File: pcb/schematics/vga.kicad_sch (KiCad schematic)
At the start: 1 part

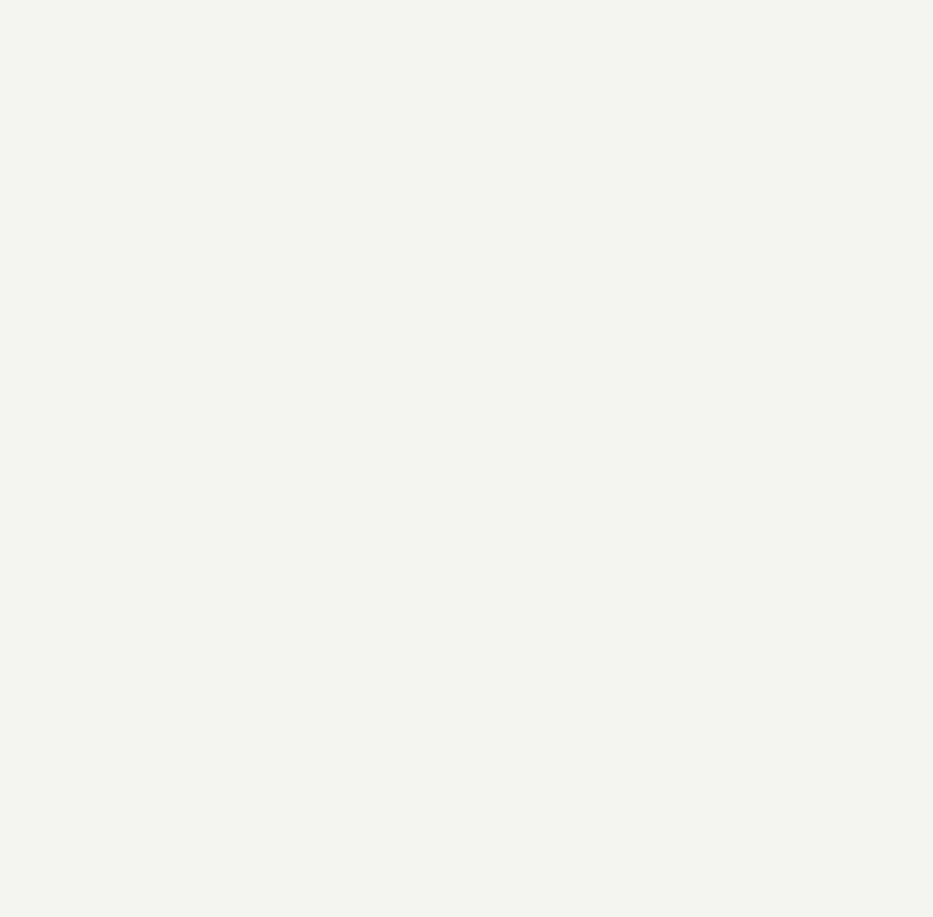
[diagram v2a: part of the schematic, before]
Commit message: add ths8136 symbol
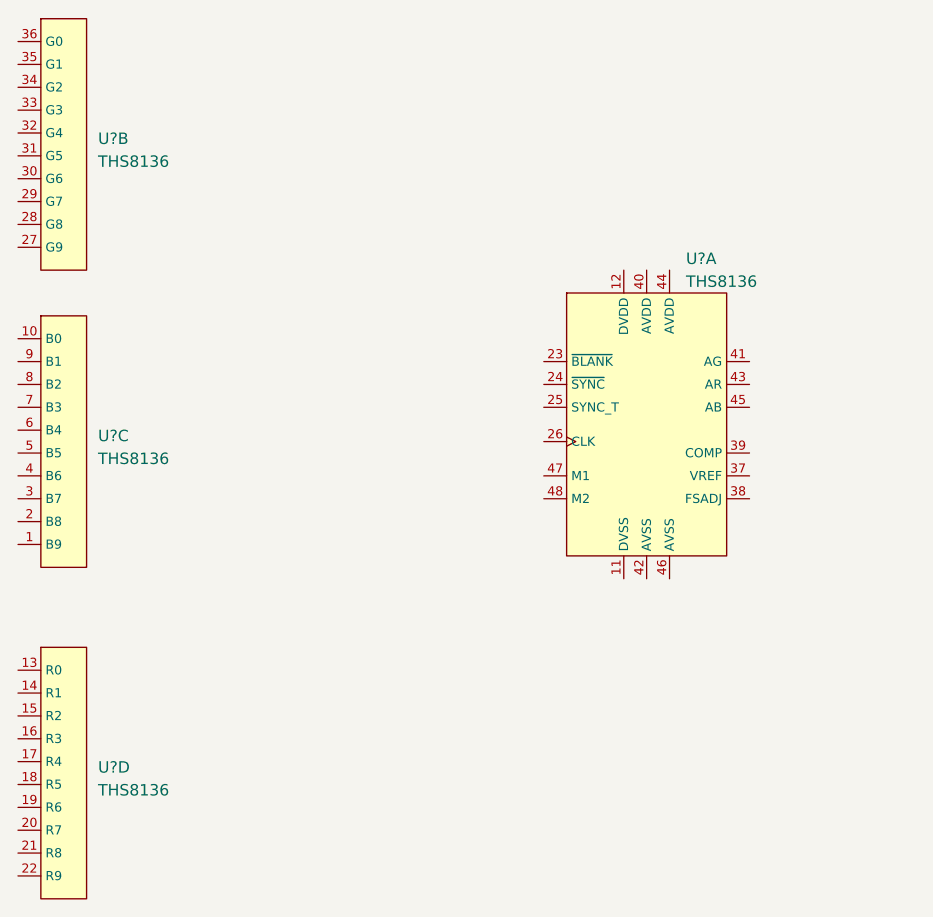
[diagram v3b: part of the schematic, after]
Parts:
- added U? (x4): THS8136, symbol THS8136:THS8136
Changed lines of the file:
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@@
 (kicad_sch (version 20220126) (generator eeschema)
   (paper "A4")
+  (symbol (lib_id "THS8136:THS8136") (at 101.6 138.43 0) (unit 4)
+    (in_bom yes) (on_board yes) (fields_autoplaced)
+    (property "Reference" "U?" (id 0) (at 102.87 127.635 0)
+      (effects (font (size 1.27 1.27)) (justify left))
+    )
+    (property "Value" "THS8136" (id 1) (at 102.87 130.175 0)
+      (effects (font (size 1.27 1.27)) (justify left))
+    )
+    (property "Footprint" "" (id 2) (at 100.33 111.76 0)
+      (effects (font (size 1.27 1.27)) hide)
+    )
+    (property "Datasheet" "" (id 3) (at 100.33 111.76 0)
+      (effects (font (size 1.27 1.27)) hide)
+    )
+    (pin "13")
+    (pin "14")
+    (pin "15")
+    (pin "16")
+    (pin "17")
+    (pin "18")
+    (pin "19")
+    (pin "20")
+    (pin "21")
+    (pin "22")
+  )
+  (symbol (lib_id "THS8136:THS8136") (at 163.83 88.9 0) (unit 1)
+    (in_bom yes) (on_board yes) (fields_autoplaced)
+    (property "Reference" "U?" (id 0) (at 168.1989 71.12 0)
+      (effects (font (size 1.27 1.27)) (justify left))
+    )
+    (property "Value" "THS8136" (id 1) (at 168.1989 73.66 0)
+      (effects (font (size 1.27 1.27)) (justify left))
+    )
+    (property "Footprint" "" (id 2) (at 162.56 62.23 0)
+      (effects (font (size 1.27 1.27)) hide)
+    )
+    (property "Datasheet" "" (id 3) (at 162.56 62.23 0)
+      (effects (font (size 1.27 1.27)) hide)
+    )
+    (pin "11")
+    (pin "12")
+    (pin "23")
+    (pin "24")
+    (pin "25")
+    (pin "26")
+    (pin "37")
+    (pin "38")
+    (pin "39")
+    (pin "40")
+    (pin "41")
+    (pin "42")
+    (pin "43")
+    (pin "44")
+    (pin "45")
+    (pin "46")
+    (pin "47")
+    (pin "48")
+  )
+  (symbol (lib_id "THS8136:THS8136") (at 101.6 68.58 0) (unit 2)
+    (in_bom yes) (on_board yes) (fields_autoplaced)
+    (property "Reference" "U?" (id 0) (at 102.87 57.785 0)
+      (effects (font (size 1.27 1.27)) (justify left))
+    )
+    (property "Value" "THS8136" (id 1) (at 102.87 60.325 0)
+      (effects (font (size 1.27 1.27)) (justify left))
+    )
+    (property "Footprint" "" (id 2) (at 100.33 41.91 0)
+      (effects (font (size 1.27 1.27)) hide)
+    )
+    (property "Datasheet" "" (id 3) (at 100.33 41.91 0)
+      (effects (font (size 1.27 1.27)) hide)
+    )
+    (pin "27")
+    (pin "28")
+    (pin "29")
+    (pin "30")
+    (pin "31")
+    (pin "32")
+    (pin "33")
+    (pin "34")
+    (pin "35")
+    (pin "36")
+  )
+  (symbol (lib_id "THS8136:THS8136") (at 101.6 101.6 0) (unit 3)
+    (in_bom yes) (on_board yes) (fields_autoplaced)
+    (property "Reference" "U?" (id 0) (at 102.87 90.805 0)
+      (effects (font (size 1.27 1.27)) (justify left))
+    )
+    (property "Value" "THS8136" (id 1) (at 102.87 93.345 0)
+      (effects (font (size 1.27 1.27)) (justify left))
+    )
+    (property "Footprint" "" (id 2) (at 100.33 74.93 0)
+      (effects (font (size 1.27 1.27)) hide)
+    )
+    (property "Datasheet" "" (id 3) (at 100.33 74.93 0)
+      (effects (font (size 1.27 1.27)) hide)
+    )
+    (pin "1")
+    (pin "10")
+    (pin "2")
+    (pin "3")
+    (pin "4")
+    (pin "5")
+    (pin "6")
+    (pin "7")
+    (pin "8")
+    (pin "9")
+  )
   (symbol (lib_id "Connector:DB15_Female_HighDensity") (at 226.06 91.44 0) (unit 1)
     (in_bom yes) (on_board yes) (fields_autoplaced)

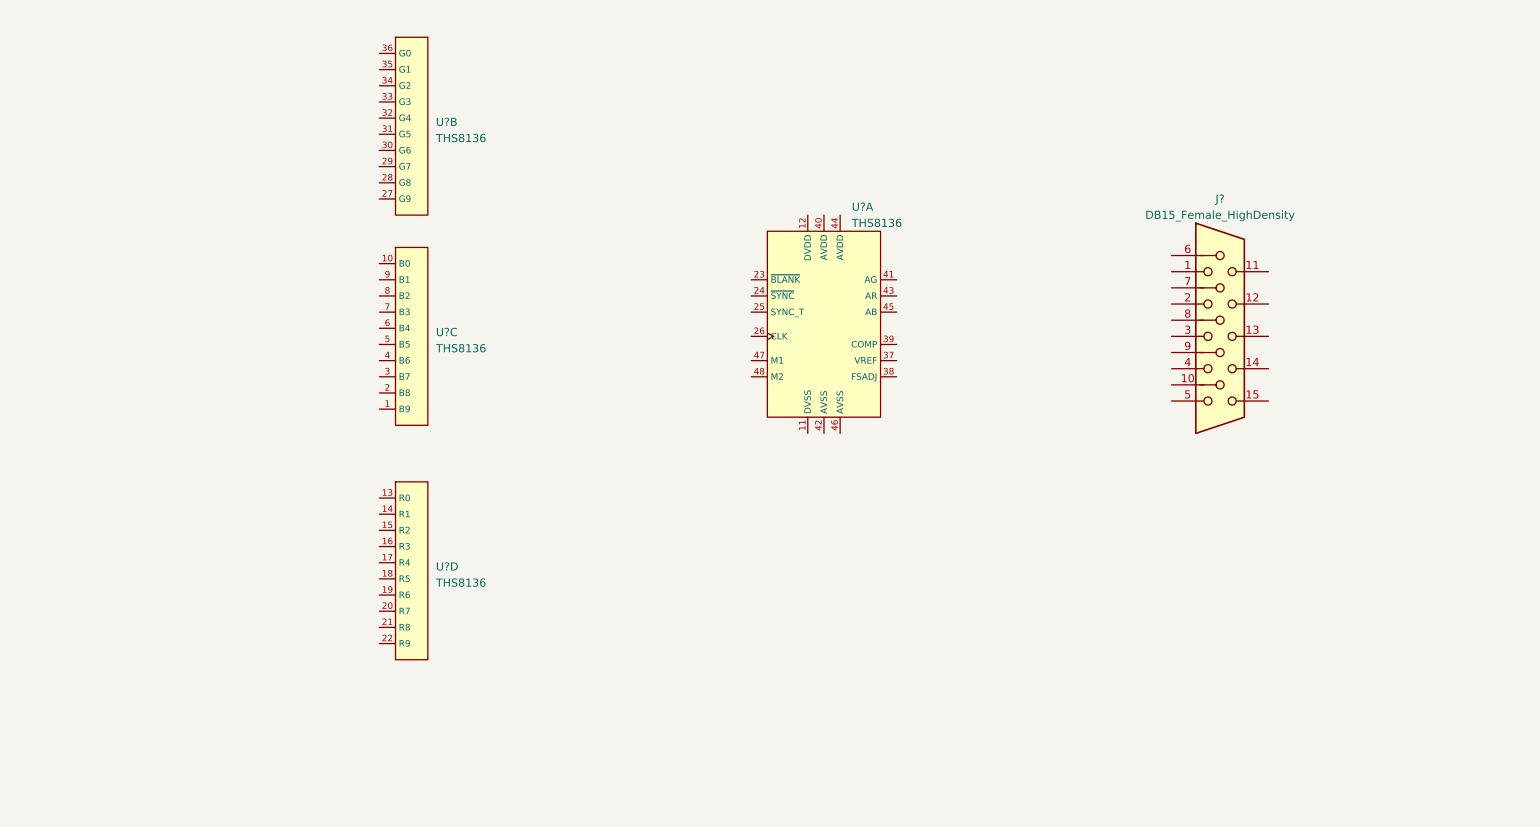
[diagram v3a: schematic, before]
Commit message: add vga frontend
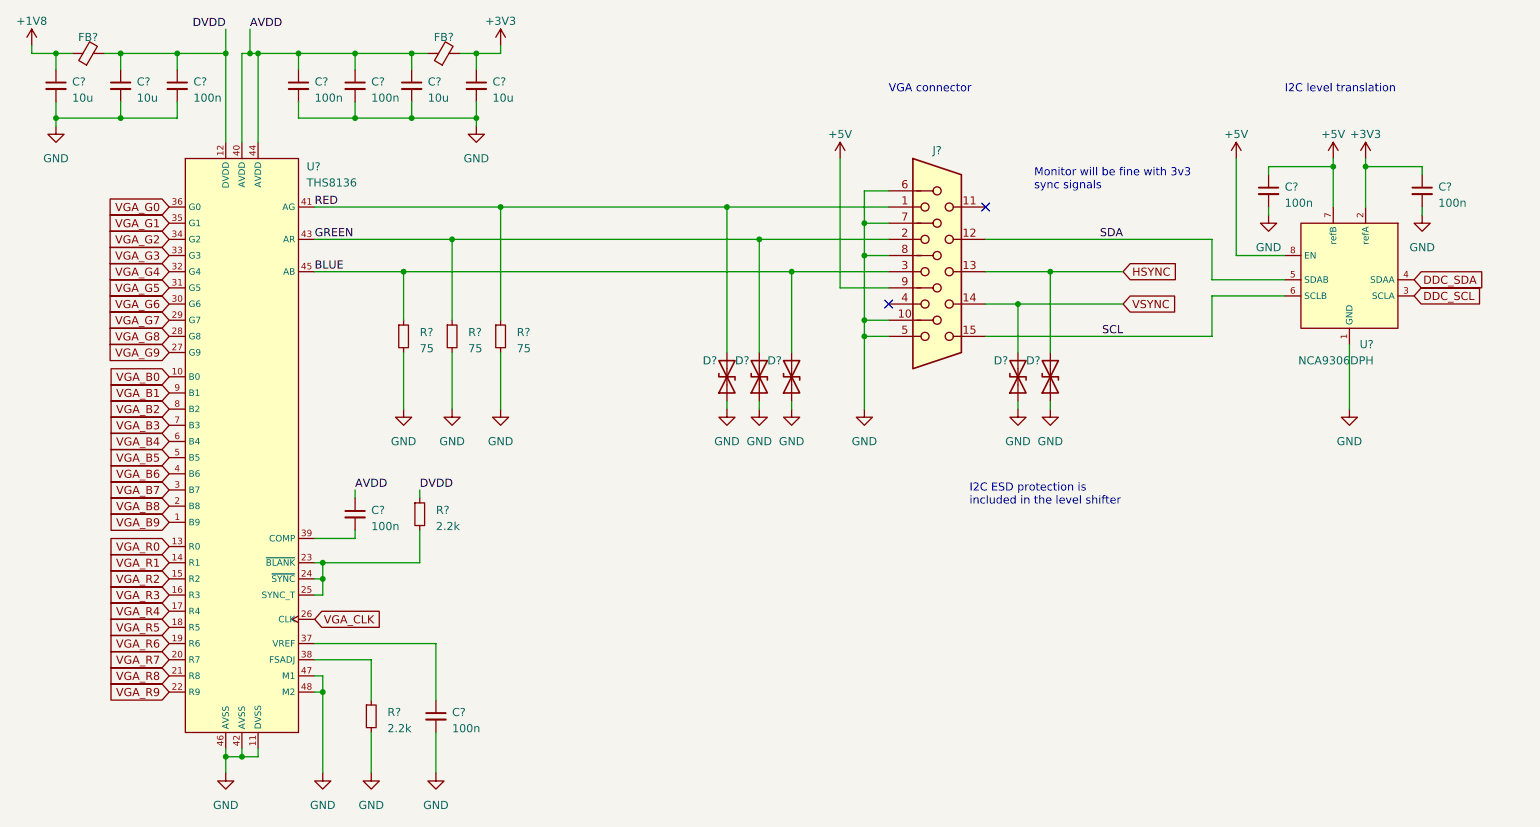
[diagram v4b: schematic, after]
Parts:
- removed U? (x4): THS8136, symbol THS8136:THS8136
- added C? (x4): 10u, symbol Device:C_Small
- added C? (x7): 100n, symbol Device:C_Small
- added D? (x5): D_TVS, symbol Device:D_TVS
- added FB? (x2): FerriteBead_Small, symbol Device:FerriteBead_Small
- added R? (x3): 75, symbol Device:R_Small
- added R? (x2): 2.2k, symbol Device:R_Small
- added U?: NCA9306DPH, symbol NCA9306:NCA9306DPH
- added U?: THS8136, symbol THS8136:THS8136
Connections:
- net RED: now reaches J?.1
- net RED: now also D?.2 (A2), R?.1, U?.41 (AG)
- net GND: now reaches J?.10
- net GND: now also J?.5, J?.6, J?.7, J?.8, C?.2, C?.2, C?.2, C?.2, C?.2, C?.2, C?.2, C?.2, C?.2, C?.2, D?.1 (A1), D?.1 (A1), D?.1 (A1), D?.1 (A1), D?.1 (A1), R?.2, R?.2, R?.2, R?.2, U?.1 (GND), U?.11 (DVSS), U?.42 (AVSS), U?.46 (AVSS), U?.47 (M1), U?.48 (M2)
- net SDA: now reaches J?.12
- net SDA: now also U?.5 (SDAB)
- net HSYNC: now reaches J?.13
- net HSYNC: now also D?.2 (A2)
- net VSYNC: now reaches J?.14
- net VSYNC: now also D?.2 (A2)
- net SCL: now reaches J?.15
- net SCL: now also U?.6 (SCLB)
- net GREEN: now reaches J?.2
- net GREEN: now also D?.2 (A2), R?.1, U?.43 (AR)
- net BLUE: now reaches J?.3
- net BLUE: now also D?.2 (A2), R?.1, U?.45 (AB)
- net +5V: now reaches J?.9
- net +5V: now also C?.1, U?.7 (refB), U?.8 (EN)
- new net: R?.2, U?.23 (~{BLANK}), U?.24 (~{SYNC}), U?.25 (SYNC_T)
- new net: C?.1, U?.37 (VREF)
- new net: R?.1, U?.38 (FSADJ)
- new net: C?.2, U?.39 (COMP)
- new net +1V8: C?.1, FB?.1
- new net +3V3: C?.1, C?.1, FB?.2, U?.2 (refA)
- new net AVDD: C?.1, C?.1, C?.1, C?.1, FB?.1, U?.40 (AVDD), U?.44 (AVDD)
- new net DDC_SCL: U?.3 (SCLA)
- new net DDC_SDA: U?.4 (SDAA)
- new net DVDD: C?.1, C?.1, FB?.2, R?.1, U?.12 (DVDD)
- new net VGA_B0: U?.10 (B0)
- new net VGA_B1: U?.9 (B1)
- new net VGA_B2: U?.8 (B2)
- new net VGA_B3: U?.7 (B3)
- new net VGA_B4: U?.6 (B4)
- new net VGA_B5: U?.5 (B5)
- new net VGA_B6: U?.4 (B6)
- new net VGA_B7: U?.3 (B7)
- new net VGA_B8: U?.2 (B8)
- new net VGA_B9: U?.1 (B9)
- new net VGA_CLK: U?.26 (CLK)
- new net VGA_G0: U?.36 (G0)
- new net VGA_G1: U?.35 (G1)
- new net VGA_G2: U?.34 (G2)
- new net VGA_G3: U?.33 (G3)
- new net VGA_G4: U?.32 (G4)
- new net VGA_G5: U?.31 (G5)
- new net VGA_G6: U?.30 (G6)
- new net VGA_G7: U?.29 (G7)
- new net VGA_G8: U?.28 (G8)
- new net VGA_G9: U?.27 (G9)
- new net VGA_R0: U?.13 (R0)
- new net VGA_R1: U?.14 (R1)
- new net VGA_R2: U?.15 (R2)
- new net VGA_R3: U?.16 (R3)
- new net VGA_R4: U?.17 (R4)
- new net VGA_R5: U?.18 (R5)
- new net VGA_R6: U?.19 (R6)
- new net VGA_R7: U?.20 (R7)
- new net VGA_R8: U?.21 (R8)
- new net VGA_R9: U?.22 (R9)
- no-connect marks 0 -> 2
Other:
- note added: "I2C ESD protection is included in the level shifter"
- note added: "I2C level translation"
- note added: "Monitor will be fine with 3v3 sync signals"
- note added: "VGA connector"
- moved on the sheet: J?

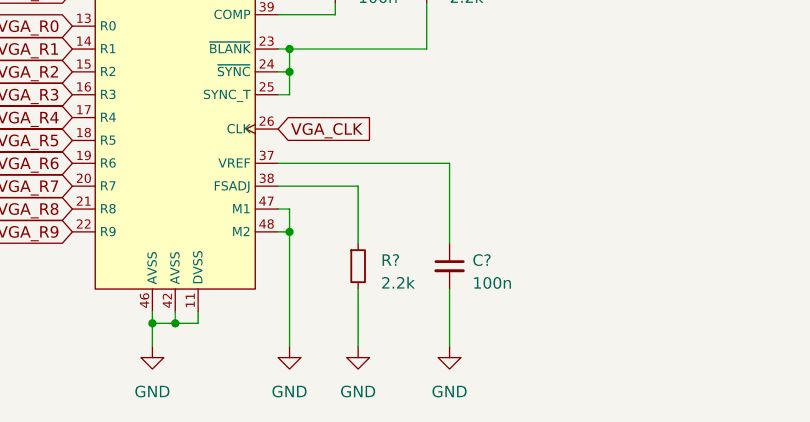
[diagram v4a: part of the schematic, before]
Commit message: fix wrong fasdj resistor on vga frontend
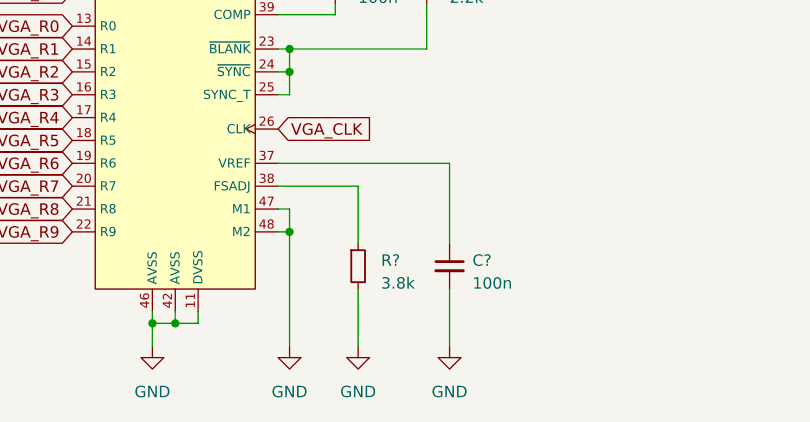
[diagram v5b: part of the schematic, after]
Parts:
- R?: value 2.2k -> 3.8k
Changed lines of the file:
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@@
       (effects (font (size 1.27 1.27)) (justify left))
     )
-    (property "Value" "2.2k" (id 1) (at 95.25 153.035 0)
+    (property "Value" "3.8k" (id 1) (at 95.25 153.035 0)
       (effects (font (size 1.27 1.27)) (justify left))
     )

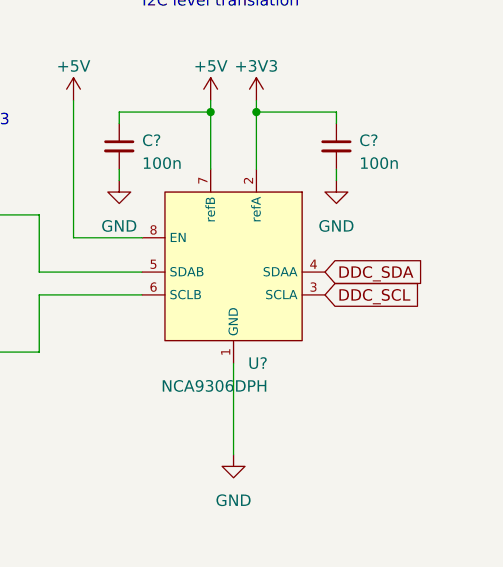
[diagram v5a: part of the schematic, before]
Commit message: add hdmi frontend
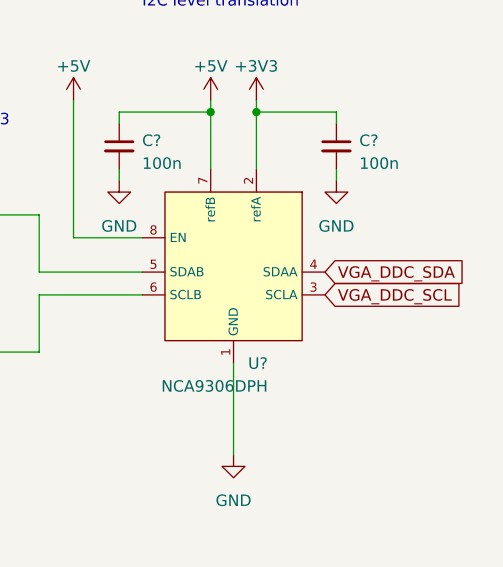
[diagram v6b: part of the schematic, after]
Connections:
- net DDC_SCL renamed VGA_DDC_SCL
- net DDC_SDA renamed VGA_DDC_SDA
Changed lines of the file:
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@@
     (effects (font (size 1.27 1.27)) (justify right bottom))
   )
-  (global_label "DDC_SCL" (shape input) (at 256.54 85.09 0) (fields_autoplaced)
+  (global_label "VGA_DDC_SCL" (shape input) (at 256.54 85.09 0) (fields_autoplaced)
     (effects (font (size 1.27 1.27)) (justify left))
-    (property "Intersheetrefs" "${INTERSHEET_REFS}" (id 0) (at 267.6673 85.09 0)
+    (property "Intersheetrefs" "${INTERSHEET_REFS}" (id 0) (at 272.0821 85.09 0)
       (effects (font (size 1.27 1.27)) (justify left))
     )
@@
     )
   )
-  (global_label "DDC_SDA" (shape input) (at 256.54 82.55 0) (fields_autoplaced)
+  (global_label "VGA_DDC_SDA" (shape input) (at 256.54 82.55 0) (fields_autoplaced)
     (effects (font (size 1.27 1.27)) (justify left))
-    (property "Intersheetrefs" "${INTERSHEET_REFS}" (id 0) (at 267.7278 82.55 0)
+    (property "Intersheetrefs" "${INTERSHEET_REFS}" (id 0) (at 272.1426 82.55 0)
       (effects (font (size 1.27 1.27)) (justify left))
     )

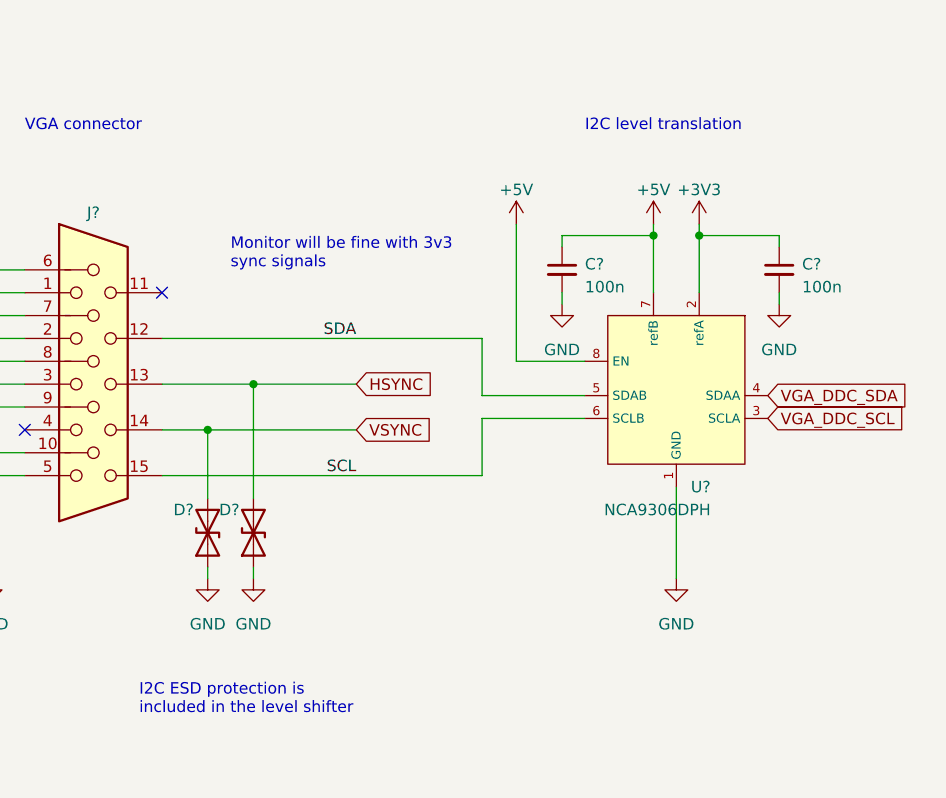
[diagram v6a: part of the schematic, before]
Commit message: add i2c mux for ddc
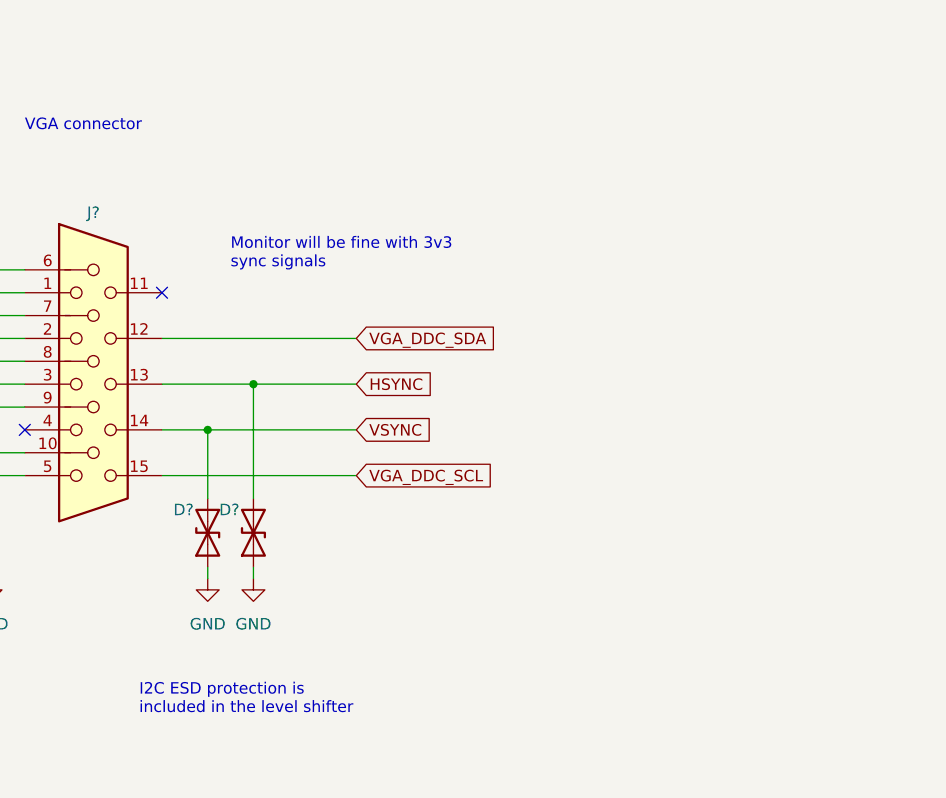
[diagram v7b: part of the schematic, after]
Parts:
- removed C? (x2): 100n, symbol Device:C_Small
- removed U?: NCA9306DPH, symbol NCA9306:NCA9306DPH
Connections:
- net SCL is gone; now on net VGA_DDC_SCL: J?.15
- net SDA is gone; now on net VGA_DDC_SDA: J?.12
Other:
- note removed: "I2C level translation"
